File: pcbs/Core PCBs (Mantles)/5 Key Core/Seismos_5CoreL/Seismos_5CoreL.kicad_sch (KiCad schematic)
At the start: 21 parts, among them J1 SM09B-SRSS-TB(LF)(SN), J2 SM09B-SRSS-TB(LF)(SN), J3 SM09B-SRSS-TB(LF)(SN), J4 SM09B-SRSS-TB(LF)(SN), J5 SM09B-SRSS-TB(LF)(SN), J6 SM09B-SRSS-TB(LF)(SN), J7 SM09B-SRSS-TB(LF)(SN), J8 MJ-4PP-9-Lily58, J9 Conn_01x05_Pin, SW1 RotaryEncoder_Switch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

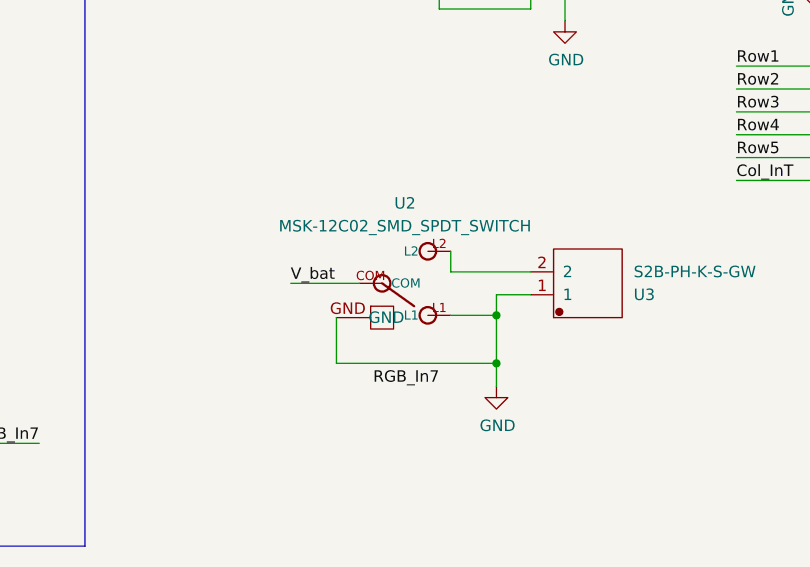
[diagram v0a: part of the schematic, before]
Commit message: Release v1.1
***NOTE***: If you have a previous commit, please update your files.
This commit fixes the incorrect RGB pinout and power switch as the
RGB footprint was incorrect.
The power switch behaviour is also fixed in this commit so the position
matches on both sides.
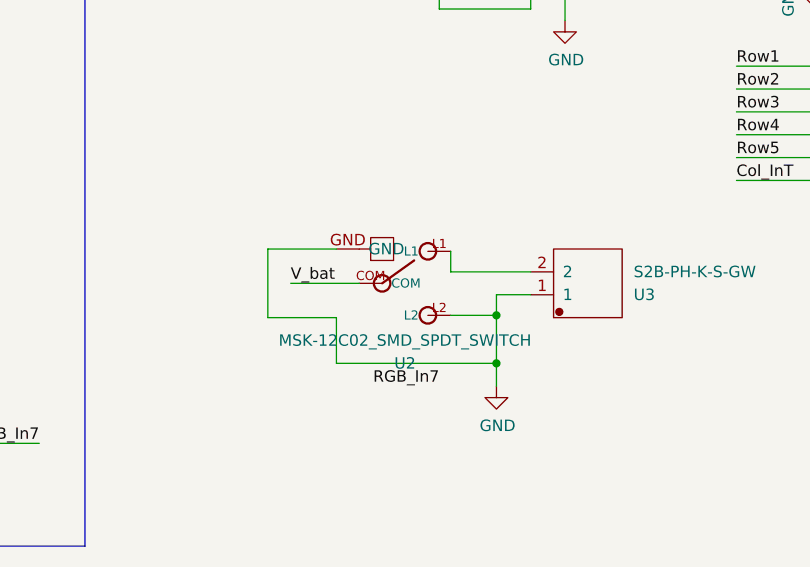
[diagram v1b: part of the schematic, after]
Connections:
- net GND: now also U2.L2; no longer U2.L1
- net at U3.2: now also U2.L1; no longer U2.L2
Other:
- moved on the sheet: U2
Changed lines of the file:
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@@
+    (stroke (width 0) (type default))
+  )
+  (wire (pts (xy 271.78 91.44) (xy 279.4 91.44))
     (stroke (width 0) (type default))
   )
@@
     (stroke (width 0) (type default))
   )
+  (wire (pts (xy 279.4 99.06) (xy 271.78 99.06))
+    (stroke (width 0) (type default))
+  )
   (wire (pts (xy 186.69 55.88) (xy 186.69 72.39))
     (stroke (width 0) (type default))
@@
   )
   (wire (pts (xy 26.67 113.03) (xy 39.37 113.03))
+    (stroke (width 0) (type default))
+  )
+  (wire (pts (xy 271.78 99.06) (xy 271.78 91.44))
     (stroke (width 0) (type default))
   )
@@
     )
   )
-  (symbol (lib_id "Seismos-sym:MSK-12C02_SMD_SPDT_SWITCH") (at 289.56 95.25 0) (unit 1)
-    (in_bom yes) (on_board yes) (dnp no) (fields_autoplaced)
-    (property "Reference" "U2" (at 287.02 86.36 0)
+  (symbol (lib_id "Seismos-sym:MSK-12C02_SMD_SPDT_SWITCH") (at 289.56 95.25 0) (mirror x) (unit 1)
+    (in_bom yes) (on_board yes) (dnp no)
+    (property "Reference" "U2" (at 287.02 104.14 0)
       (effects (font (size 1.27 1.27)))
     )
-    (property "Value" "MSK-12C02_SMD_SPDT_SWITCH" (at 287.02 88.9 0)
+    (property "Value" "MSK-12C02_SMD_SPDT_SWITCH" (at 287.02 101.6 0)
       (effects (font (size 1.27 1.27)))
     )

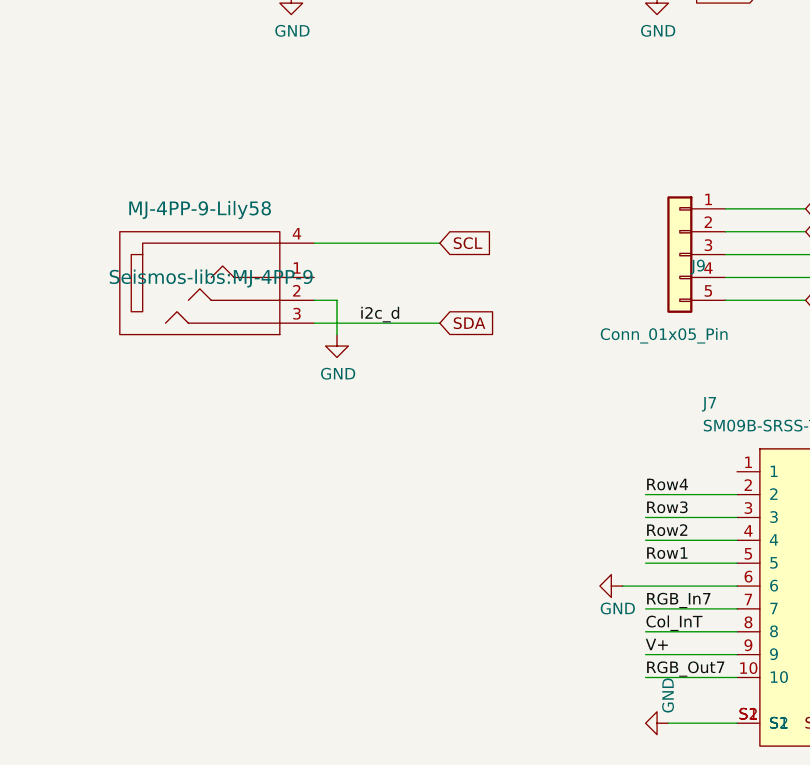
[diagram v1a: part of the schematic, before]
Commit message: Release v1.1.1
Added I2C pull up resistors and bridge contacts on the backif 5V power
is desired. If you have v1.1, V+ is actually close to the headphone
jack, so you can scratch off the trace and bridge there.
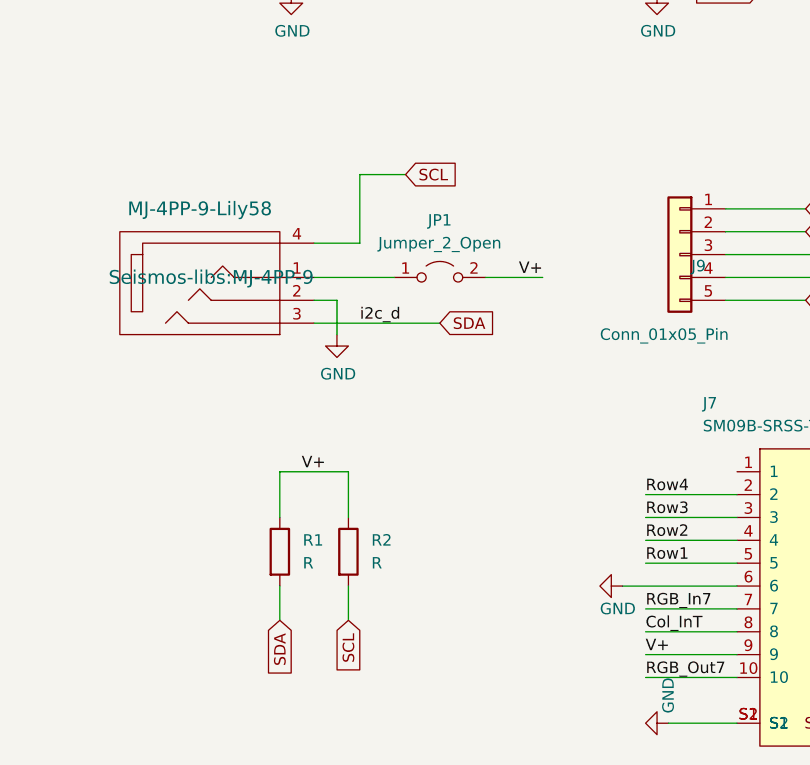
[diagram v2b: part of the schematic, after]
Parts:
- added JP1: Jumper_2_Open, Jumper:SolderJumper-2_P1.3mm_Open_TrianglePad1.0x1.5mm, symbol Seismos-sym:Jumper_2_Open
- added R1, R2: R, Resistor_SMD:R_0603_1608Metric_Pad0.98x0.95mm_HandSolder, symbol Seismos-sym:Resistor
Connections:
- net SCL: now also R2.2
- net SDA: now also R1.2
- net V+: now also JP1.2 (B), R1.1, R2.1
- net at J8.1: now also JP1.1 (A)
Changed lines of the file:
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@@
+    (stroke (width 0) (type default))
+  )
+  (wire (pts (xy 318.77 138.43) (xy 325.12 138.43))
     (stroke (width 0) (type default))
   )
@@
     (stroke (width 0) (type default))
   )
-  (wire (pts (xy 299.72 134.62) (xy 313.69 134.62))
+  (wire (pts (xy 304.8 127) (xy 309.88 127))
+    (stroke (width 0) (type default))
+  )
+  (wire (pts (xy 299.72 138.43) (xy 308.61 138.43))
     (stroke (width 0) (type default))
   )
@@
     (stroke (width 0) (type default))
   )
+  (wire (pts (xy 304.8 134.62) (xy 299.72 134.62))
+    (stroke (width 0) (type default))
+  )
   (wire (pts (xy 373.38 55.88) (xy 381 55.88))
     (stroke (width 0) (type default))
   )
+  (wire (pts (xy 303.53 172.72) (xy 303.53 176.53))
+    (stroke (width 0) (type default))
+  )
   (wire (pts (xy 156.21 113.03) (xy 166.37 113.03))
     (stroke (width 0) (type default))
@@
     (stroke (width 0) (type default))
   )
+  (wire (pts (xy 295.91 160.02) (xy 295.91 165.1))
+    (stroke (width 0) (type default))
+  )
   (wire (pts (xy 224.79 55.88) (xy 224.79 72.39))
     (stroke (width 0) (type default))
@@
     (stroke (width 0) (type default))
   )
+  (wire (pts (xy 303.53 160.02) (xy 303.53 165.1))
+    (stroke (width 0) (type default))
+  )
   (wire (pts (xy 102.87 55.88) (xy 102.87 72.39))
     (stroke (width 0) (type default))
@@
     (stroke (width 0) (type default))
   )
+  (wire (pts (xy 295.91 172.72) (xy 295.91 176.53))
+    (stroke (width 0) (type default))
+  )
   (wire (pts (xy 29.21 55.88) (xy 29.21 72.39))
     (stroke (width 0) (type default))
@@
     (stroke (width 0) (type default))
   )
+  (wire (pts (xy 304.8 127) (xy 304.8 134.62))
+    (stroke (width 0) (type default))
+  )
   (wire (pts (xy 279.4 99.06) (xy 271.78 99.06))
     (stroke (width 0) (type default))
@@
   )
   (wire (pts (xy 148.59 55.88) (xy 148.59 72.39))
+    (stroke (width 0) (type default))
+  )
+  (wire (pts (xy 295.91 160.02) (xy 303.53 160.02))
     (stroke (width 0) (type default))
   )
@@
     (effects (font (size 1.27 1.27)) (justify right bottom))
   )
+  (label "V+" (at 300.99 160.02 180) (fields_autoplaced)
+    (effects (font (size 1.27 1.27)) (justify right bottom))
+  )
   (label "Col_In1" (at 41.91 72.39 90) (fields_autoplaced)
     (effects (font (size 1.27 1.27)) (justify left bottom))
@@
   (label "RGB_In5" (at 191.77 72.39 90) (fields_autoplaced)
     (effects (font (size 1.27 1.27)) (justify left bottom))
+  )
+  (label "V+" (at 325.12 138.43 180) (fields_autoplaced)
+    (effects (font (size 1.27 1.27)) (justify right bottom))
   )
   (label "Col_In6" (at 389.89 83.82 180) (fields_autoplaced)
@@
     )
   )
-  (global_label "SCL" (shape input) (at 313.69 134.62 0)
+  (global_label "SCL" (shape input) (at 309.88 127 0)
     (effects (font (size 1.27 1.27)) (justify left))
-    (property "Intersheetrefs" "${INTERSHEET_REFS}" (at 313.69 134.62 0)
+    (property "Intersheetrefs" "${INTERSHEET_REFS}" (at 309.88 127 0)
       (effects (font (size 1.27 1.27)) hide)
     )
@@
     (property "Intersheetrefs" "${INTERSHEET_REFS}" (at 373.38 68.58 0)
       (effects (font (size 1.27 1.27)) hide)
+    )
+  )
+  (global_label "SCL" (shape input) (at 303.53 176.53 270) (fields_autoplaced)
+    (effects (font (size 1.27 1.27)) (justify right))
+    (property "Intersheetrefs" "${INTERSHEET_REFS}" (at 303.53 183.0228 90)
+      (effects (font (size 1.27 1.27)) (justify right) hide)
+    )
+  )
+  (global_label "SDA" (shape input) (at 295.91 176.53 270) (fields_autoplaced)
+    (effects (font (size 1.27 1.27)) (justify right))
+    (property "Intersheetrefs" "${INTERSHEET_REFS}" (at 295.91 183.0833 90)
+      (effects (font (size 1.27 1.27)) (justify right) hide)
     )
   )
@@
     )
   )
+  (symbol (lib_id "Seismos-sym:Resistor") (at 295.91 168.91 0) (unit 1)
+    (in_bom yes) (on_board yes) (dnp no) (fields_autoplaced)
+    (property "Reference" "R1" (at 298.45 167.64 0)
+      (effects (font (size 1.27 1.27)) (justify left))
+    )
+    (property "Value" "R" (at 298.45 170.18 0)
+      (effects (font (size 1.27 1.27)) (justify left))
+    )
+    (property "Footprint" "Resistor_SMD:R_0603_1608Metric_Pad0.98x0.95mm_HandSolder" (at 294.132 168.91 90)
+      (effects (font (size 1.27 1.27)) hide)
+    )
+    (property "Datasheet" "~" (at 295.91 168.91 0)
+      (effects (font (size 1.27 1.27)) hide)
+    )
+    (pin "1")
+    (pin "2")
+    (instances
+      (project "Seismos_5CoreL"
+        (path "/c801d42e-dd94-493e-bd2f-6c3ddad43f55"
+          (reference "R1") (unit 1)
+        )
+      )
+    )
+  )
   (symbol (lib_id "Seismos-sym:SM10B-SRSS-TB_(LF)(SN)") (at 353.06 175.26 0) (unit 1)
     (in_bom yes) (on_board yes) (dnp no)
@@
     )
   )
+  (symbol (lib_id "Seismos-sym:Jumper_2_Open") (at 313.69 138.43 0) (unit 1)
+    (in_bom yes) (on_board yes) (dnp no) (fields_autoplaced)
+    (property "Reference" "JP1" (at 313.69 132.08 0)
+      (effects (font (size 1.27 1.27)))
+    )
+    (property "Value" "Jumper_2_Open" (at 313.69 134.62 0)
+      (effects (font (size 1.27 1.27)))
+    )
+    (property "Footprint" "Jumper:SolderJumper-2_P1.3mm_Open_TrianglePad1.0x1.5mm" (at 313.69 138.43 0)
+      (effects (font (size 1.27 1.27)) hide)
+    )
+    (property "Datasheet" "~" (at 313.69 138.43 0)
+      (effects (font (size 1.27 1.27)) hide)
+    )
+    (pin "1")
+    (pin "2")
+    (instances
+      (project "Seismos_5CoreL"
+        (path "/c801d42e-dd94-493e-bd2f-6c3ddad43f55"
+          (reference "JP1") (unit 1)
+        )
+      )
+    )
+  )
   (symbol (lib_id "Seismos-sym:MJ-4PP-9-Lily58") (at 288.29 138.43 0) (unit 1)
     (in_bom yes) (on_board yes) (dnp no)
@@
         )
       )
+    )
+  )
+  (symbol (lib_id "Seismos-sym:Resistor") (at 303.53 168.91 0) (unit 1)
+    (in_bom yes) (on_board yes) (dnp no) (fields_autoplaced)
+    (property "Reference" "R2" (at 306.07 167.64 0)
+      (effects (font (size 1.27 1.27)) (justify left))
+    )
+    (property "Value" "R" (at 306.07 170.18 0)
+      (effects (font (size 1.27 1.27)) (justify left))
+    )
+    (property "Footprint" "Resistor_SMD:R_0603_1608Metric_Pad0.98x0.95mm_HandSolder" (at 301.752 168.91 90)
+      (effects (font (size 1.27 1.27)) hide)
+    )
+    (property "Datasheet" "~" (at 303.53 168.91 0)
+      (effects (font (size 1.27 1.27)) hide)
+    )
+    (pin "1")
+    (pin "2")
+    (instances
+      (project "Seismos_5CoreL"
+        (path "/c801d42e-dd94-493e-bd2f-6c3ddad43f55"
+          (reference "R2") (unit 1)
+        )
+      )

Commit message: Fix right encoder button, fix connector refs
Right side encoder was still connected to the 6th column for some
reason... Figures when you copy paste the same board design into a
different project.

Also fixed references for the SH connectors, so it doesn't look weird
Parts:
- J1, J2, J3, J4, J5, J6: value SM09B-SRSS-TB(LF)(SN) -> SM010B-SRSS-TB(LF)(SN)
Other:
- note added: "Bottom Connectors"
- note removed: "Top Connectors"
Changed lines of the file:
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@@
     (effects (font (size 1.27 1.27)) (justify left top))
   )
-  (text "Top Connectors" (at 73.66 31.75 0)
+  (text "Bottom Connectors" (at 62.23 31.75 0)
     (effects (font (size 10 10)) (justify left bottom))
   )
@@
       (effects (font (size 1.27 1.27)) (justify left))
     )
-    (property "Value" "SM09B-SRSS-TB(LF)(SN)" (at 242.57 41.91 90)
+    (property "Value" "SM010B-SRSS-TB(LF)(SN)" (at 242.57 41.91 90)
       (effects (font (size 1.27 1.27)) (justify left))
     )
@@
       (effects (font (size 1.27 1.27)) (justify left))
     )
-    (property "Value" "SM09B-SRSS-TB(LF)(SN)" (at 204.47 41.91 90)
+    (property "Value" "SM010B-SRSS-TB(LF)(SN)" (at 204.47 41.91 90)
       (effects (font (size 1.27 1.27)) (justify left))
     )
@@
       (effects (font (size 1.27 1.27)) (justify left))
     )
-    (property "Value" "SM09B-SRSS-TB(LF)(SN)" (at 128.27 41.91 90)
+    (property "Value" "SM010B-SRSS-TB(LF)(SN)" (at 128.27 41.91 90)
       (effects (font (size 1.27 1.27)) (justify left))
     )
@@
       (effects (font (size 1.27 1.27)) (justify left))
     )
-    (property "Value" "SM09B-SRSS-TB(LF)(SN)" (at 52.07 41.91 90)
+    (property "Value" "SM010B-SRSS-TB(LF)(SN)" (at 52.07 41.91 90)
       (effects (font (size 1.27 1.27)) (justify left))
     )
@@
       (effects (font (size 1.27 1.27)) (justify left))
     )
-    (property "Value" "SM09B-SRSS-TB(LF)(SN)" (at 166.37 41.91 90)
+    (property "Value" "SM010B-SRSS-TB(LF)(SN)" (at 166.37 41.91 90)
       (effects (font (size 1.27 1.27)) (justify left))
     )
@@
       (effects (font (size 1.27 1.27)) (justify left))
     )
-    (property "Value" "SM09B-SRSS-TB(LF)(SN)" (at 90.17 41.91 90)
-      (effects (font (size 1.27 1.27)) (justify left))
-    )
+    (property "Value" "SM010B-SRSS-TB(LF)(SN)" (at 90.17 41.91 90)
+      (effects (font (size 1.27 1.27)) (justify left))
+    )

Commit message: Added 74HC595A support, new release
New PCB versions supporting shift register.
Another JST SH connector is added to expose 2 spare pins.

Footprints for microcontroller were updated using modified footprint from library.
Original variants updated to these new footprints with some fixes as well.
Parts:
- J7: value SM09B-SRSS-TB(LF)(SN) -> SM10B-SRSS-TB_(LF)(SN)
- U1: footprint keyboard_reversible:ProMicro -> Seismos-libs:keebRev-onesided_ProMicro
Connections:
- net GND: now also SW1.MP
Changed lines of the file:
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@@
+    (stroke (width 0) (type default))
+  )
+  (wire (pts (xy 375.92 96.52) (xy 368.3 96.52))
     (stroke (width 0) (type default))
   )
@@
     )
   )
-  (symbol (lib_name "GND_1") (lib_id "power:GND") (at 36.83 58.42 0) (mirror y) (unit 1)
+  (symbol (lib_id "power:GND") (at 36.83 58.42 0) (mirror y) (unit 1)
     (in_bom yes) (on_board yes) (dnp no)
     (property "Reference" "#PWR012" (at 36.83 64.77 0)
@@
     (pin "B")
     (pin "C")
+    (pin "MP")
     (pin "S1")
     (pin "S2")
@@
       (effects (font (size 1.27 1.27)))
     )
-    (property "Footprint" "keyboard_reversible:ProMicro" (at 355.6 67.31 0)
+    (property "Footprint" "Seismos-libs:keebRev-onesided_ProMicro" (at 355.6 67.31 0)
       (effects (font (size 1.27 1.27)) hide)
     )
@@
     )
   )
-  (symbol (lib_name "GND_1") (lib_id "power:GND") (at 74.93 58.42 0) (mirror y) (unit 1)
+  (symbol (lib_id "power:GND") (at 74.93 58.42 0) (mirror y) (unit 1)
     (in_bom yes) (on_board yes) (dnp no)
     (property "Reference" "#PWR01" (at 74.93 64.77 0)
@@
     )
   )
-  (symbol (lib_name "GND_1") (lib_id "power:GND") (at 113.03 58.42 0) (mirror y) (unit 1)
+  (symbol (lib_id "power:GND") (at 113.03 58.42 0) (mirror y) (unit 1)
     (in_bom yes) (on_board yes) (dnp no)
     (property "Reference" "#PWR03" (at 113.03 64.77 0)
@@
     )
   )
-  (symbol (lib_name "GND_1") (lib_id "power:GND") (at 189.23 58.42 0) (mirror y) (unit 1)
+  (symbol (lib_id "power:GND") (at 189.23 58.42 0) (mirror y) (unit 1)
     (in_bom yes) (on_board yes) (dnp no)
     (property "Reference" "#PWR018" (at 189.23 64.77 0)
@@
     )
   )
+  (symbol (lib_id "power:GND") (at 375.92 96.52 90) (mirror x) (unit 1)
+    (in_bom yes) (on_board yes) (dnp no)
+    (property "Reference" "#PWR03" (at 382.27 96.52 0)
+      (effects (font (size 1.27 1.27)) hide)
+    )
+    (property "Value" "GND" (at 379.1712 96.647 90)
+      (effects (font (size 1.27 1.27)) (justify right))
+    )
+    (property "Footprint" "" (at 375.92 96.52 0)
+      (effects (font (size 1.27 1.27)) hide)
+    )
+    (property "Datasheet" "" (at 375.92 96.52 0)
+      (effects (font (size 1.27 1.27)) hide)
+    )
+    (pin "1")
+    (instances
+      (project "KeysOnRails_Carrier1"
+        (path "/a6dae978-c8fe-4bbf-835b-e2bd64164dfb"
+          (reference "#PWR03") (unit 1)
+        )
+      )
+      (project "Seismos_5CoreL"
+        (path "/c801d42e-dd94-493e-bd2f-6c3ddad43f55"
+          (reference "#PWR026") (unit 1)
+        )
+      )
+    )
+  )
   (symbol (lib_id "power:GND") (at 128.27 60.96 0) (unit 1)
     (in_bom yes) (on_board yes) (dnp no)
@@
     )
   )
-  (symbol (lib_name "GND_1") (lib_id "power:GND") (at 151.13 58.42 0) (mirror y) (unit 1)
+  (symbol (lib_id "power:GND") (at 151.13 58.42 0) (mirror y) (unit 1)
     (in_bom yes) (on_board yes) (dnp no)
     (property "Reference" "#PWR06" (at 151.13 64.77 0)
@@
       (effects (font (size 1.27 1.27)) (justify left))
     )
-    (property "Value" "SM09B-SRSS-TB(LF)(SN)" (at 342.9 154.94 0)
+    (property "Value" "SM10B-SRSS-TB_(LF)(SN)" (at 342.9 154.94 0)
       (effects (font (size 1.27 1.27)) (justify left))
     )
@@
     )
   )
-  (symbol (lib_name "GND_1") (lib_id "power:GND") (at 227.33 58.42 0) (mirror y) (unit 1)
+  (symbol (lib_id "power:GND") (at 227.33 58.42 0) (mirror y) (unit 1)
     (in_bom yes) (on_board yes) (dnp no)
     (property "Reference" "#PWR023" (at 227.33 64.77 0)

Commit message: HOTFIX, power switch bridges to ground
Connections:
- net GND: no longer U2.L2
